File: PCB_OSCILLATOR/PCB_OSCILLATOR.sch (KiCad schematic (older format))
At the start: 96 parts, among them J1 Jumper, J10 Jumper, J11 Jumper, J12 Jumper, J13 Jumper, J14 Jumper, J15 Jumper, J16 Jumper, J2 Jumper, J3 Jumper, J4 Jumper, J5 Jumper, J6 Jumper, J7 Jumper, J8 Jumper, J9 Jumper, P1 POWER SUPPLY, P2 SPI_AD5270_1, P3 SPI_AD5270_2, P4 SPI_AD9833_1, P5 SPI_AD9833_2, U1 AD5270, U10 ADR291, U2 AD8421, U3 AD9833, U4 AD5270, U5 AD8421, U6 AD9833, U7 ADG819, U8 ADP3303, U9 AD8651

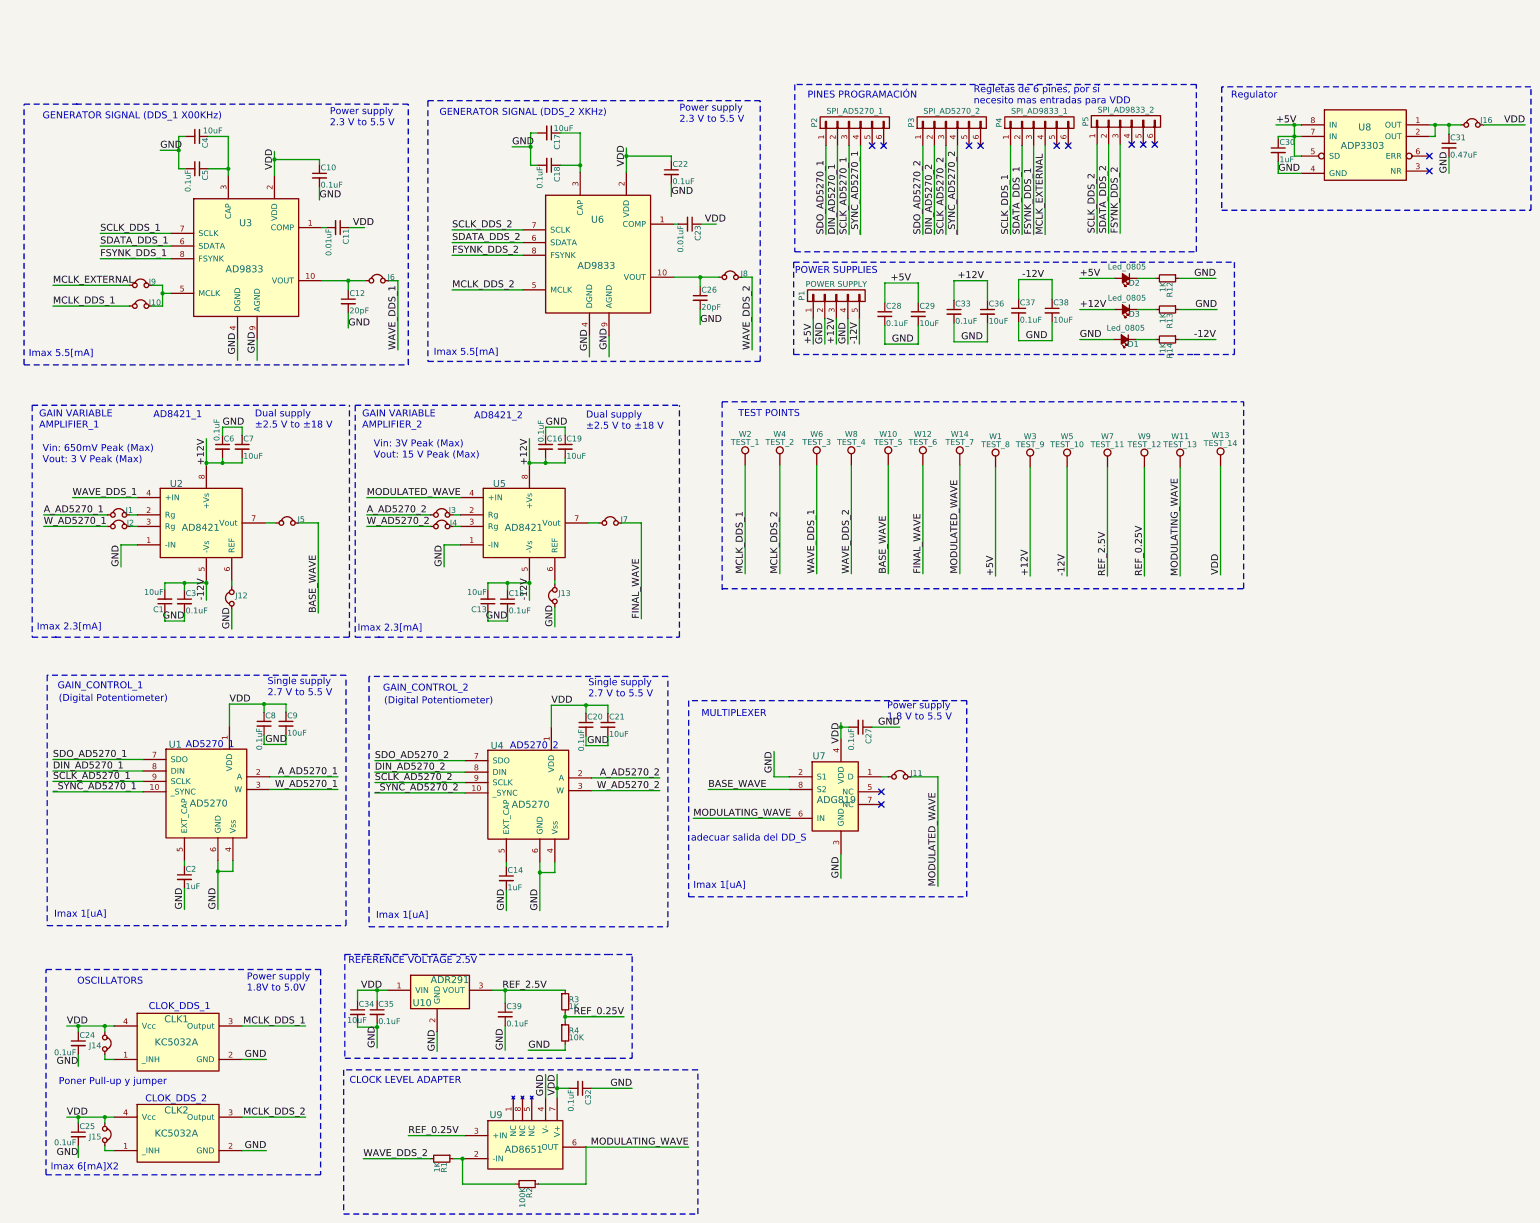
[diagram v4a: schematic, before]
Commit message: Pequeñas correciones
Cambio de Huellas de capacitores
Correción de footPrint de jumpers con errores
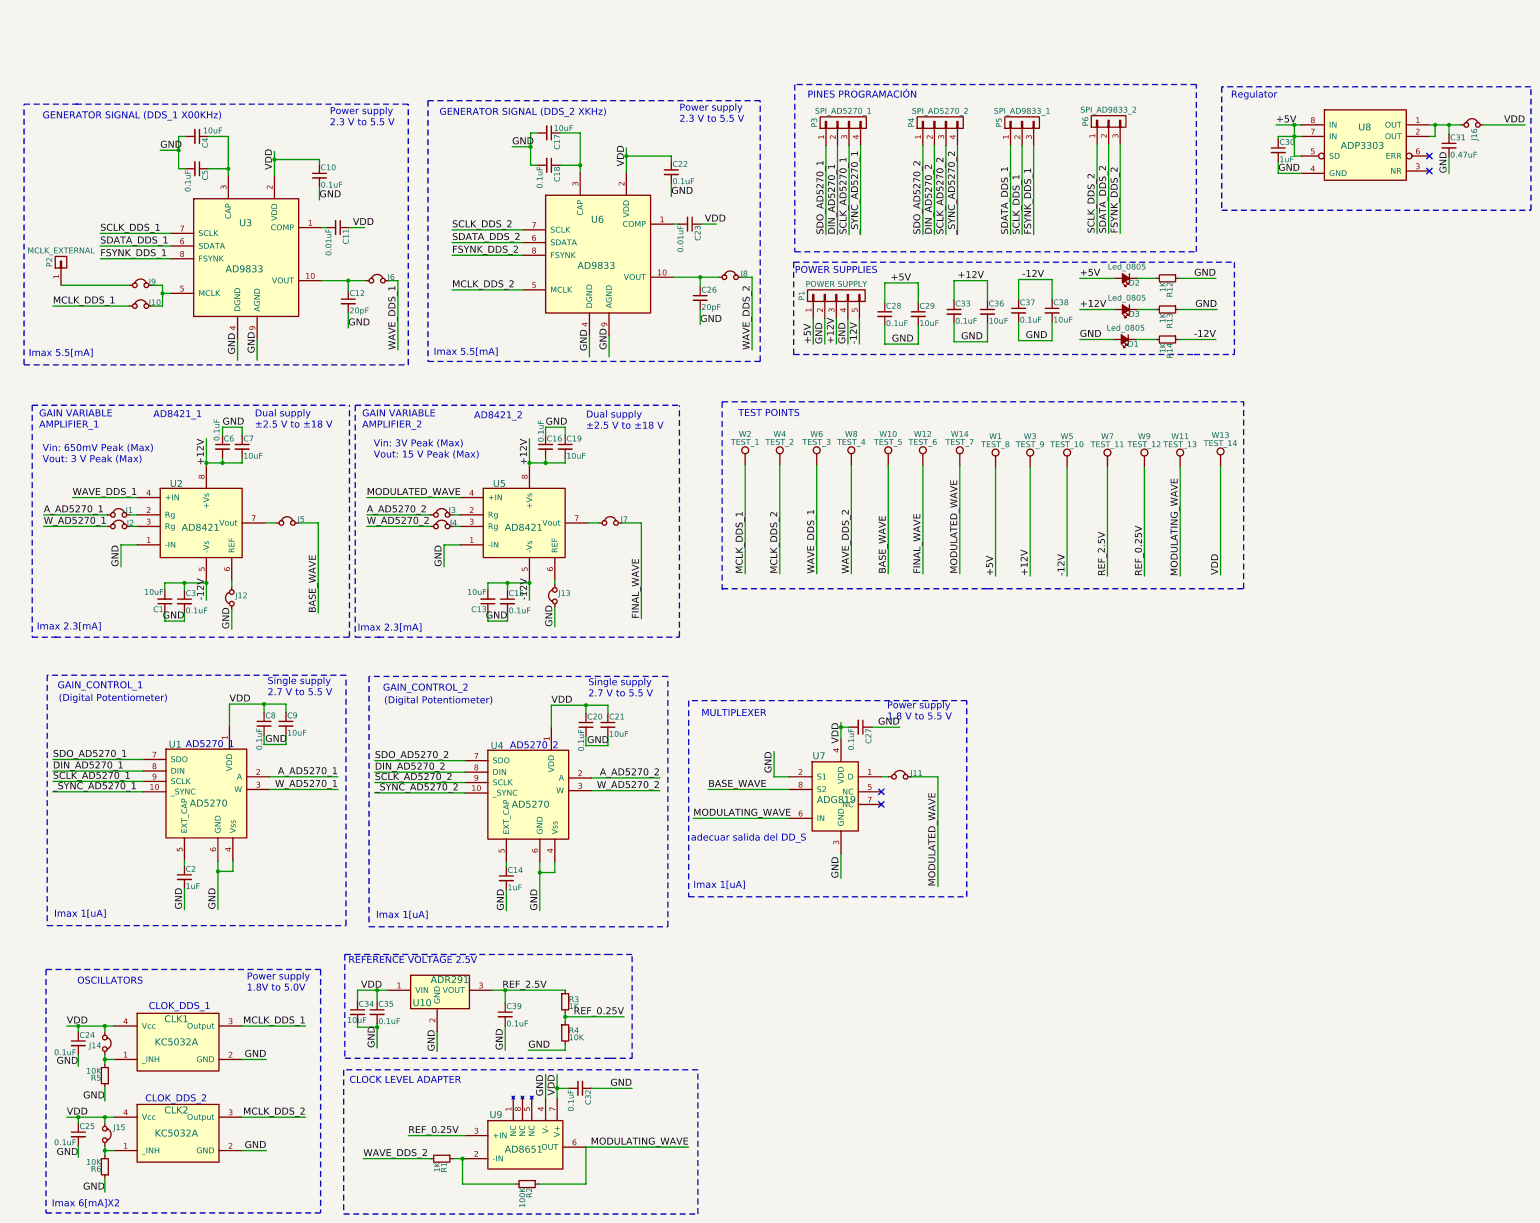
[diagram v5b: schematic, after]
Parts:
- removed P2: SPI_AD5270_1, Socket_Strips:Socket_Strip_Straight_1x06, symbol CONN_01X06
- removed P3: SPI_AD5270_2, Socket_Strips:Socket_Strip_Straight_1x06, symbol CONN_01X06
- removed P4: SPI_AD9833_1, Socket_Strips:Socket_Strip_Straight_1x06, symbol CONN_01X06
- removed P5: SPI_AD9833_2, Socket_Strips:Socket_Strip_Straight_1x06, symbol CONN_01X06
- added P2: MCLK_EXTERNAL, Socket_Strips:Socket_Strip_Straight_1x01, symbol CONN_01X01
- added P3: SPI_AD5270_1, Socket_Strips:Socket_Strip_Straight_1x04, symbol CONN_01X04
- added P4: SPI_AD5270_2, Socket_Strips:Socket_Strip_Straight_1x04, symbol CONN_01X04
- added P5: SPI_AD9833_1, Socket_Strips:Socket_Strip_Straight_1x03, symbol CONN_01X03
- added P6: SPI_AD9833_2, Socket_Strips:Socket_Strip_Straight_1x03, symbol CONN_01X03
- added R5, R6: 10K, Resistors_SMD:R_0805_HandSoldering, symbol 10K
- C10, C11, C12, C14, C15, C16, C17, C18, C2, C20, C22, C23, C24, C25, C26, C27, C28, C29, C3, C32, C33, C34, C35, C36, C37, C38, C39, C4, C5, C6, C8, C9: footprint Resistors_SMD:R_0805_HandSoldering -> Capacitors_SMD:C_0805_HandSoldering
- C21: footprint Resistors_SMD:R_0805_HandSoldering -> Capacitors_SMD:C_1206_HandSoldering
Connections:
- net DIN_AD5270_1: now also P3.2 (P2)
- net DIN_AD5270_2: now also P4.2 (P2)
- net FSYNK_DDS_1: now also P5.3 (P3)
- net FSYNK_DDS_2: now also P6.3 (P3)
- net GND: now also R5.1, R6.1
- net SCLK_AD5270_1: now also P3.3 (P3)
- net SCLK_AD5270_2: now also P4.3 (P3)
- net SCLK_DDS_1: now also P5.2 (P2)
- net SCLK_DDS_2: now also P6.1 (P1)
- net SDATA_DDS_1: now also P5.1 (P1)
- net SDATA_DDS_2: now also P6.2 (P2)
- net SDO_AD5270_1: now also P3.1 (P1)
- net SDO_AD5270_2: now also P4.1 (P1)
- net _SYNC_AD5270_1: now also P3.4 (P4)
- net _SYNC_AD5270_2: now also P4.4 (P4)
- net at CLK1.1 (_INH), J14.1: now also R5.2
- net at CLK2.1 (_INH), J15.1: now also R6.2
- net MCLK_EXTERNAL: no longer names the net of J9.2
- net MCLK_EXTERNAL: now also P2.1 (P1)
- no-connect marks 13 -> 4
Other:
- note removed: "Poner Pull-up y jumper"
- note removed: "Regletas de 6 pines, por si \nnecesito mas entradas para VDD"

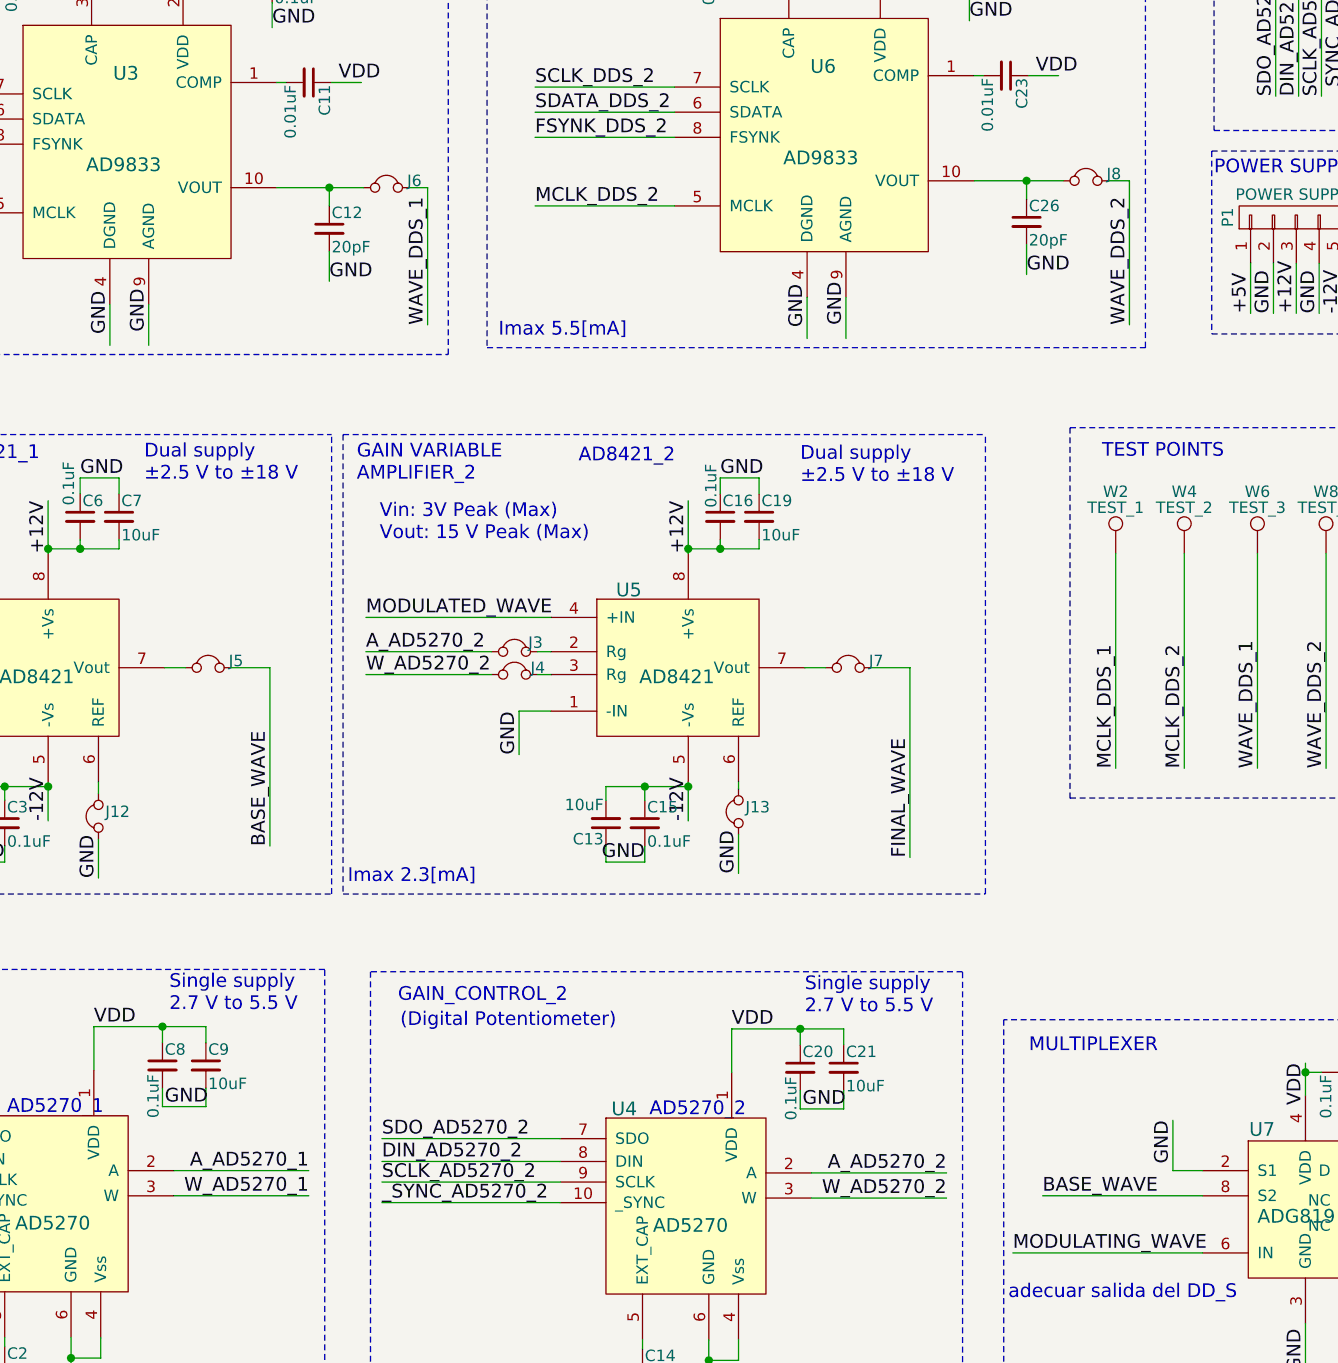
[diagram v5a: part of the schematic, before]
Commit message: Inicio de borrador de ruteado
//
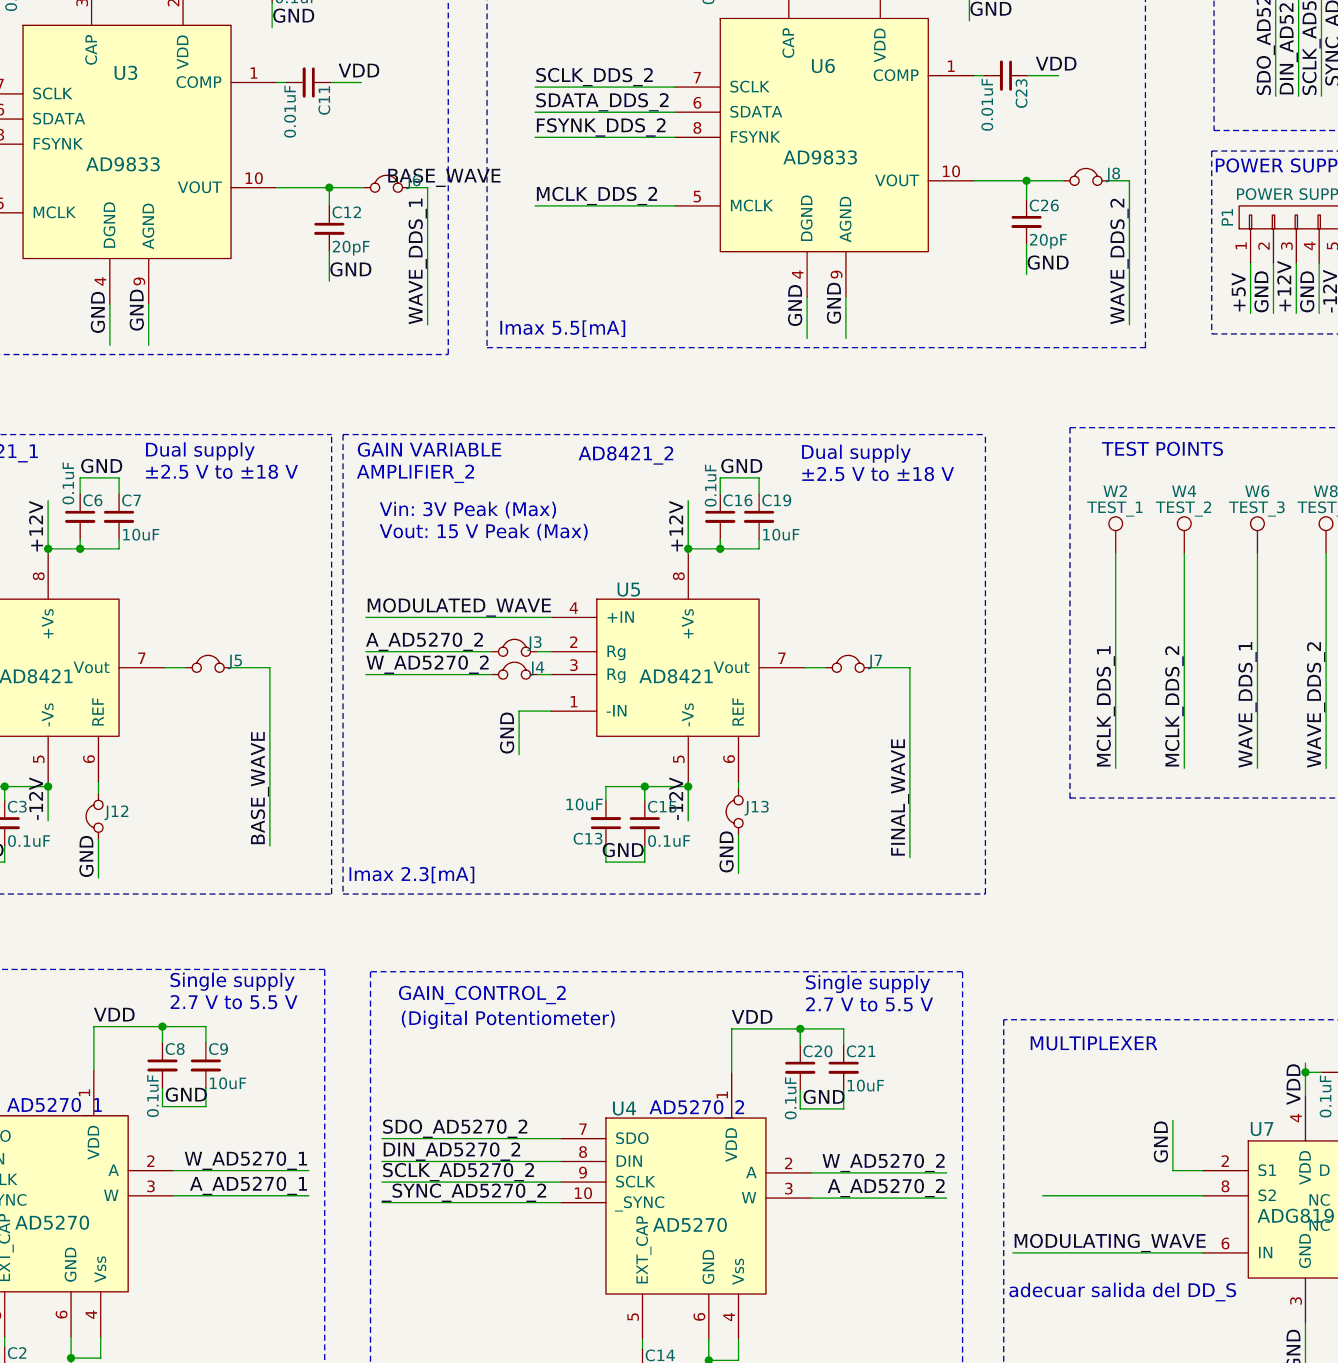
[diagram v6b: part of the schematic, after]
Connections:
- net A_AD5270_1: now also U1.3 (W); no longer U1.2 (A)
- net A_AD5270_2: now also U4.3 (W); no longer U4.2 (A)
- net BASE_WAVE: no longer U7.8 (S2)
- net W_AD5270_1: now also U1.2 (A); no longer U1.3 (W)
- net W_AD5270_2: now also U4.2 (A); no longer U4.3 (W)
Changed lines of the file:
@@
 Text Label 3360 5270 1    60   ~ 0
 BASE_WAVE
-Text Label 6740 6800 0    60   ~ 0
+Text Label 3870 2390 0    60   ~ 0
 BASE_WAVE
 Text Label 7120 2990 1    60   ~ 0
@@
 Text Label 1060 6820 0    60   ~ 0
 _SYNC_AD5270_1
+Text Label 3530 6800 2    60   ~ 0
+A_AD5270_1
 Text Label 3530 6690 2    60   ~ 0
-A_AD5270_1
-Text Label 3530 6800 2    60   ~ 0
 W_AD5270_1
 Text Notes 1100 5940 0    60   ~ 0
@@
 Text Label 3850 6830 0    60   ~ 0
 _SYNC_AD5270_2
+Text Label 6320 6810 2    60   ~ 0
+A_AD5270_2
 Text Label 6320 6700 2    60   ~ 0
-A_AD5270_2
-Text Label 6320 6810 2    60   ~ 0
 W_AD5270_2
 Text Notes 2210 6450 0    60   ~ 0

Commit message: Board al 70%
// =)
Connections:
- net BASE_WAVE: now also U7.8 (S2)
- net SCLK_DDS_2: now also P6.2 (P2); no longer P6.1 (P1)
- net SDATA_DDS_2: now also P6.1 (P1); no longer P6.2 (P2)
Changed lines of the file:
@@
 Text Label 9560 1990 1    60   ~ 0
 FSYNK_DDS_1
+Text Label 10210 1980 1    60   ~ 0
+SCLK_DDS_2
 Text Label 10110 1980 1    60   ~ 0
-SCLK_DDS_2
-Text Label 10210 1980 1    60   ~ 0
 SDATA_DDS_2
 Text Label 10310 1980 1    60   ~ 0
@@
 	1    0    0    -1
 $EndComp
+Text Label 6740 6800 0    60   ~ 0
+BASE_WAVE
 $EndSCHEMATC
